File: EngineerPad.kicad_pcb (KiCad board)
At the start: 2 copper layers, 67 parts, among them J1 AVR ISP, SW1 SW_Push, SW10 SW_Push, SW11 SW_Push, SW12 SW_Push, SW13 SW_Push, SW14 SW_Push, SW15 SW_Push, SW16 SW_Push, SW17 SW_Push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

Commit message: layout change
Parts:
- moved F1 17.3 mm to (152.0, 51.8)
- moved C3 16.5 mm to (149.9, 45.0)
- moved D24 14.1 mm to (134.3, 51.2)
- moved D25 14.1 mm to (137.7, 51.2)
- moved USB1 4.48 mm to (138.0, 41.0)
- moved D26 2.93 mm to (149.5, 39.4)

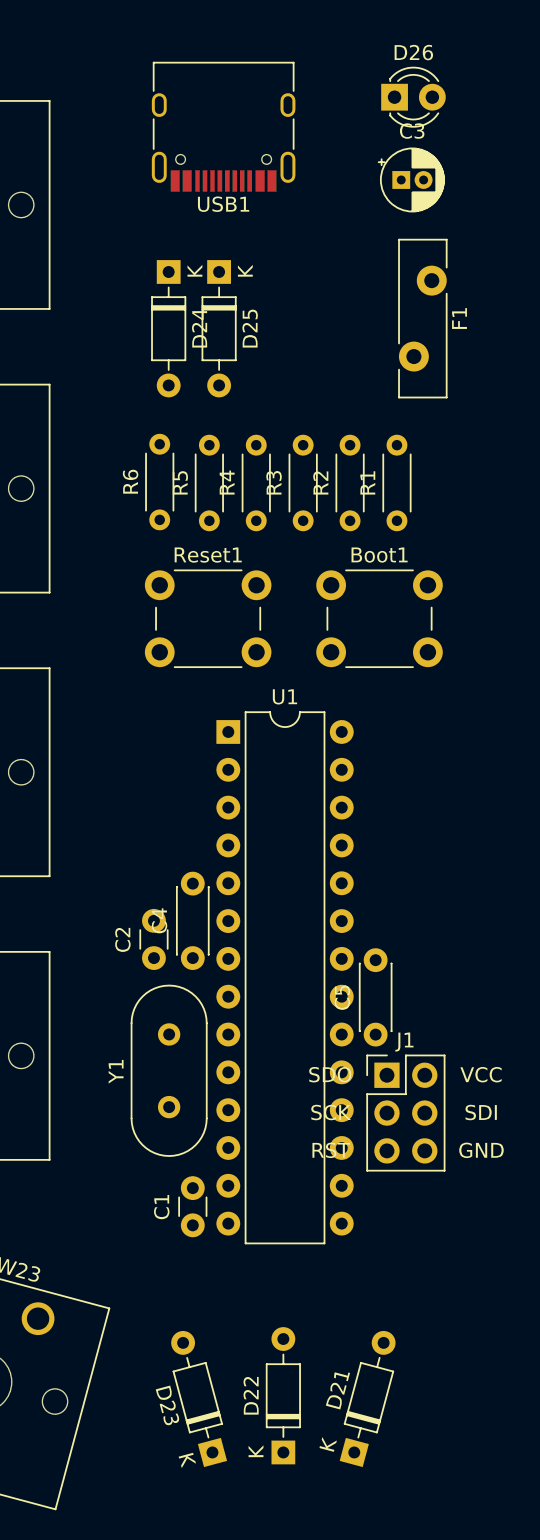
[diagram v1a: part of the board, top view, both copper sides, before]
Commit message: remove boot
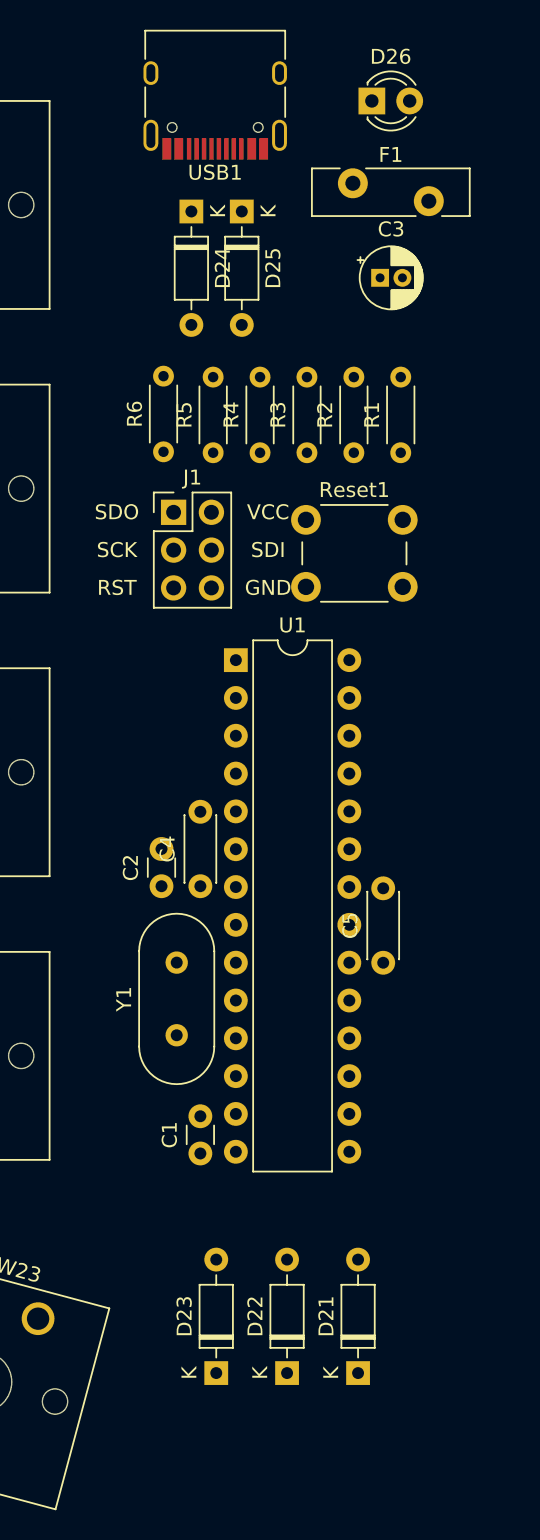
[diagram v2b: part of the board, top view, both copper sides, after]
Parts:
- removed Boot1: Boot, Button_Switch_THT:SW_PUSH_6mm
- moved J1 40.4 mm to (134.6, 67.3)
- moved Reset1 10.8 mm to (143.5, 67.8)
- moved F1 8.42 mm to (146.7, 45.2), turned to 0 degrees
- moved C3 6.72 mm to (148.5, 51.6)
- moved D23 5.34 mm to (137.5, 125.1), turned to 90 degrees
- moved D21 5.34 mm to (147.0, 125.1), turned to 90 degrees
- moved D22 5.34 mm to (142.2, 125.1)
- moved C1 4.85 mm to (136.4, 110.4)
- moved C5 4.85 mm to (148.7, 97.6)
- moved Y1 4.85 mm to (134.8, 102.4)
- moved C4 4.85 mm to (136.4, 92.4)
- moved C2 4.85 mm to (133.8, 92.4)
- moved U1 4.85 mm to (138.8, 77.2)
- moved R5 4.58 mm to (137.3, 63.3)
- moved R1 4.58 mm to (149.9, 63.3)
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
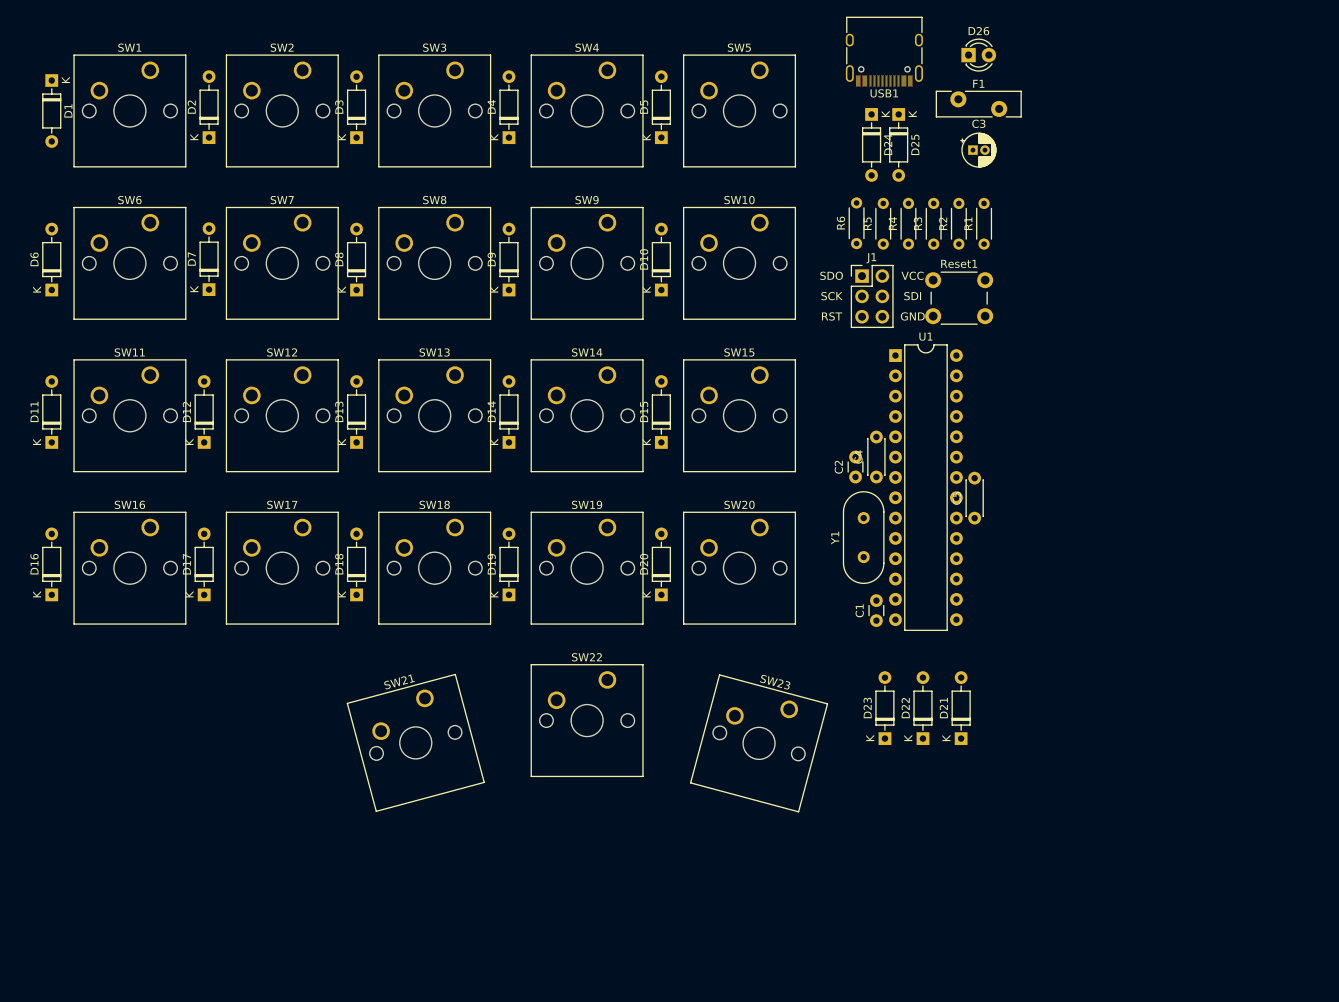
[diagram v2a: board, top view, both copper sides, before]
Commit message: switch to type a receptacle
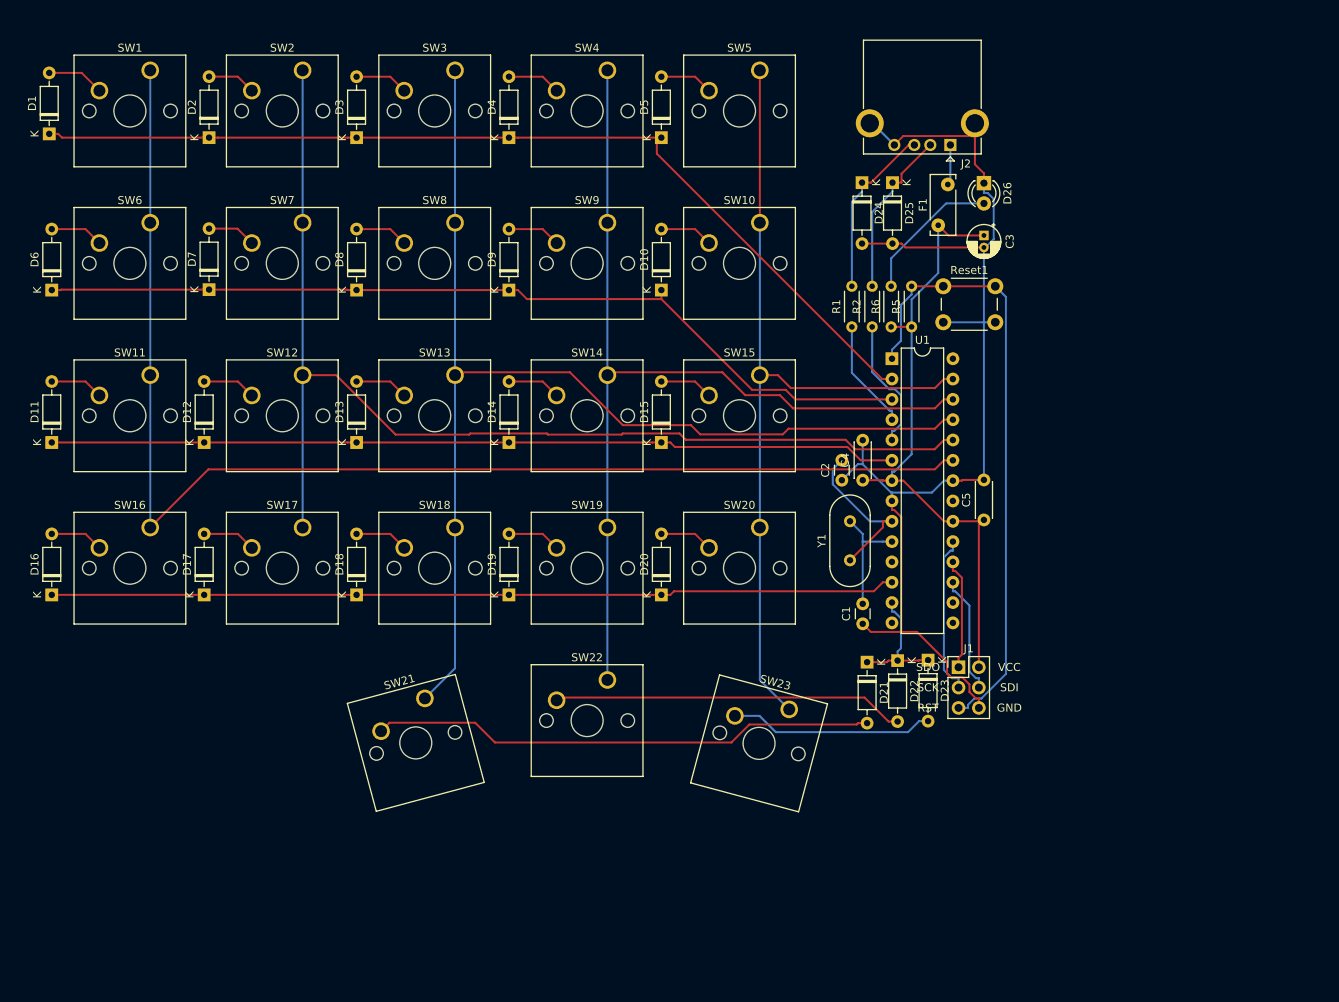
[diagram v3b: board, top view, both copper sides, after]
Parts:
- removed R3, R4: 5.1K, Resistor_THT:R_Axial_DIN0204_L3.6mm_D1.6mm_P5.08mm_Horizontal
- removed USB1: TYPE-C, JSA:USB_C_Receptacle_HRO_TYPE-C-31-M-12
- added J2: USB_A, Connector_USB:USB_A_CONNFLY_DS1095-WNR0, F.Cu at (145.7, 50.9)
- F1: footprint Fuse:Fuse_Bourns_MF-RG500 -> Fuse:Fuse_Bourns_MF-RHT050
- moved J1 50.4 mm to (146.7, 116.2)
- moved R1 19.5 mm to (133.3, 73.7)
- moved D26 16.1 mm to (149.9, 55.7), turned to 270 degrees
- moved F1 15.9 mm to (144.1, 61.0), turned to 90 degrees
- moved D21 15.1 mm to (135.3, 115.6), turned to 270 degrees
- moved R2 15.0 mm to (135.9, 73.7)
- moved R6 11.3 mm to (138.3, 73.7)
- moved D23 11.2 mm to (142.9, 115.3), turned to 270 degrees
- moved R5 10.9 mm to (140.8, 73.7)
- moved C3 10.8 mm to (149.9, 62.2), turned to 270 degrees
- moved D22 10.3 mm to (139.1, 115.4), turned to 270 degrees
- moved D24 8.60 mm to (134.6, 55.6)
- moved D25 8.55 mm to (138.4, 55.6)
- moved D1 6.68 mm to (33.0, 49.5), turned to 90 degrees
- moved C1 1.76 mm to (134.7, 110.8)
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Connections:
- net /DP renamed Net-(D24-Pad1)
- D25 pad 1: /DN -> Net-(D25-Pad1)
- F1 pad 2: /VSUB -> Net-(F1-Pad2)
- R2 pad 1: /DN -> D-
- R2 pad 2: D- -> Net-(D25-Pad1)
- U1 pad 11: Boot -> (no net)
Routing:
- net Col0: track 0.00 -> 161.0 mm
- net Col2: track 0.00 -> 146.4 mm
- net GND: track 0.00 -> 145.8 mm
- net Col1: track 0.00 -> 143.0 mm
- net Col3: track 0.00 -> 121.9 mm
- net Row0: track 0.00 -> 119.8 mm
- net Row1: track 0.00 -> 111.9 mm
- net Col4: track 0.00 -> 106.7 mm
- net Row2: track 0.00 -> 105.9 mm
- net Row3: track 0.00 -> 105.7 mm
- net +5V: track 0.00 -> 78.9 mm
- net Reset: track 0.00 -> 77.4 mm
- net Net-(D21-Pad2): track 0.00 -> 63.2 mm
- net Net-(D22-Pad2): track 0.00 -> 44.0 mm
- net Net-(D23-Pad2): track 0.00 -> 25.6 mm
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
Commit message: socket and low profile
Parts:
- SW21, SW22, SW23: footprint Button_Switch_Keyboard:SW_Cherry_MX_1.00u_PCB -> JSA:SW_PG1350
- U1: footprint Package_DIP:DIP-28_W7.62mm -> Package_DIP:DIP-28_W7.62mm_Socket
- moved SW23 8.26 mm to (119.4, 127.0)
- moved SW21 7.03 mm to (81.3, 127.0)
- moved SW22 5.73 mm to (100.1, 122.9)
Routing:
- net Col0: track 161.0 -> 0.00 mm
- net Col2: track 146.4 -> 0.00 mm
- net GND: track 145.8 -> 0.00 mm
- net Col1: track 143.0 -> 0.00 mm
- net Col3: track 121.9 -> 0.00 mm
- net Row0: track 119.8 -> 0.00 mm
- net Row1: track 111.9 -> 0.00 mm
- net Col4: track 106.7 -> 0.00 mm
- net Row2: track 105.9 -> 0.00 mm
- net Row3: track 105.7 -> 0.00 mm
- net +5V: track 78.9 -> 0.00 mm
- net Reset: track 77.4 -> 0.00 mm
- net Net-(D21-Pad2): track 63.2 -> 0.00 mm
- net Net-(D22-Pad2): track 44.0 -> 0.00 mm
- net Net-(D23-Pad2): track 25.6 -> 0.00 mm
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
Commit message: first layout
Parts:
- added R3: 1.5k, Resistor_THT:R_Axial_DIN0204_L3.6mm_D1.6mm_P5.08mm_Horizontal, F.Cu at (138.4, 72.4)
- moved D23 11.5 mm to (131.6, 117.3)
- moved D25 7.08 mm to (135.9, 62.2), turned to 90 degrees
- moved D24 6.73 mm to (133.3, 62.2), turned to 90 degrees
- moved Y1 5.05 mm to (133.3, 97.8), turned to 270 degrees
- moved D22 4.41 mm to (135.1, 117.3)
- moved D21 3.86 mm to (138.7, 117.3)
- moved R6 2.99 mm to (141.0, 72.4)
- moved R5 2.97 mm to (143.5, 72.4)
- moved Reset1 2.84 mm to (147.3, 67.3)
- moved C2 2.65 mm to (132.1, 90.2), turned to 270 degrees
- moved F1 1.91 mm to (142.2, 61.0)
- moved J1 1.88 mm to (145.8, 117.9)
- moved C3 1.80 mm to (148.6, 61.0)
- moved D26 1.67 mm to (148.6, 54.6)
- moved R1 1.27 mm to (133.3, 72.4)
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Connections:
- net Net-(D24-Pad1) renamed /DP
- net Net-(D25-Pad1) renamed /DN
- J1 pad 1: SDO -> Row1
- J1 pad 3: SCK -> Row0
- J1 pad 4: SDI -> Row2
- U1 pad 12: Row3 -> (no net)
- U1 pad 13: Row4 -> (no net)
- U1 pad 15: (no net) -> Row4
- U1 pad 16: (no net) -> Row3
- U1 pad 17: SDI -> Row2
- U1 pad 18: SDO -> Row1
- U1 pad 19: SCK -> Row0
- U1 pad 2: Row0 -> (no net)
- U1 pad 23: Col0 -> Col4
- U1 pad 24: Col1 -> Col3
- U1 pad 26: Col3 -> Col1
- U1 pad 27: Col4 -> Col0
- U1 pad 3: Row1 -> (no net)
- U1 pad 4: D+ -> D-
- U1 pad 5: D- -> D+
- U1 pad 6: Row2 -> (no net)
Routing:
- net Col0: track 0.00 -> 239.0 mm
- net Col1: track 0.00 -> 227.1 mm
- net Row0: track 0.00 -> 213.0 mm
- net Col2: track 0.00 -> 210.4 mm
- net Col3: track 0.00 -> 188.7 mm
- net Row1: track 0.00 -> 186.4 mm
- net Col4: track 0.00 -> 180.9 mm
- net Reset: track 0.00 -> 156.5 mm
- net Row2: track 0.00 -> 155.7 mm
- net Row3: track 0.00 -> 119.8 mm
- net +5V: track 0.00 -> 90.3 mm
- net Net-(D21-Pad2): track 0.00 -> 64.8 mm
- net Net-(D22-Pad2): track 0.00 -> 45.0 mm
- net /DN: track 0.00 -> 23.3 mm
- net Net-(D23-Pad2): track 0.00 -> 20.7 mm
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- added copper zone on B.Cu, net GND
- added copper zone on F.Cu, net GND
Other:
- net class Power added: clearance 0.2, trace_width 0.5, via_dia 0.8, via_drill 0.4

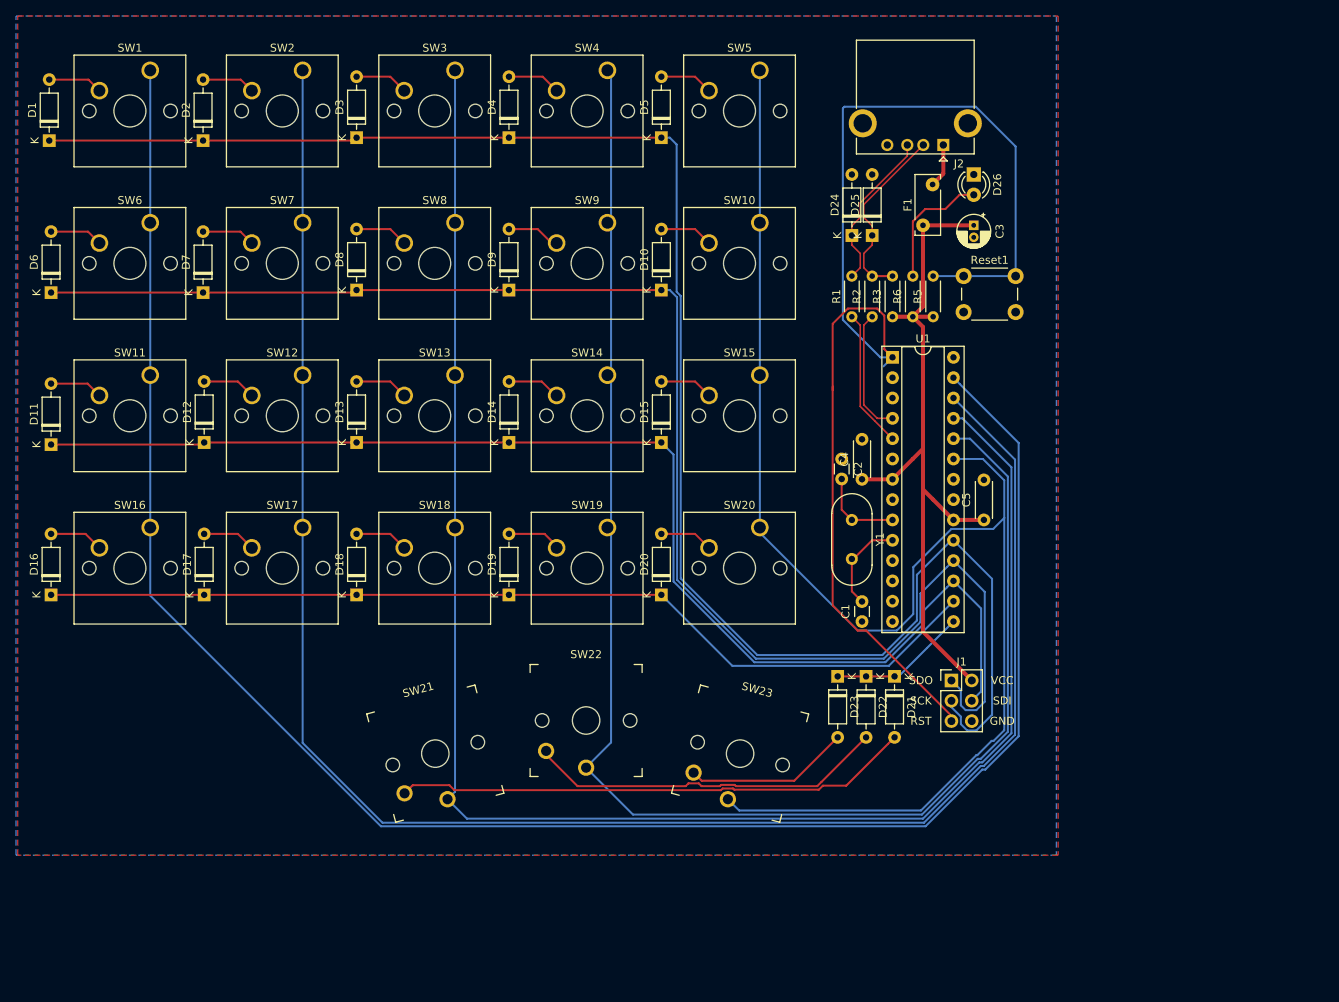
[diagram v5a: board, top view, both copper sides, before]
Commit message: Form factor 因為要做成5mm邊框切齊鍵帽，因此PCB從鍵帽處內縮1mm，外殼預計是5mm。
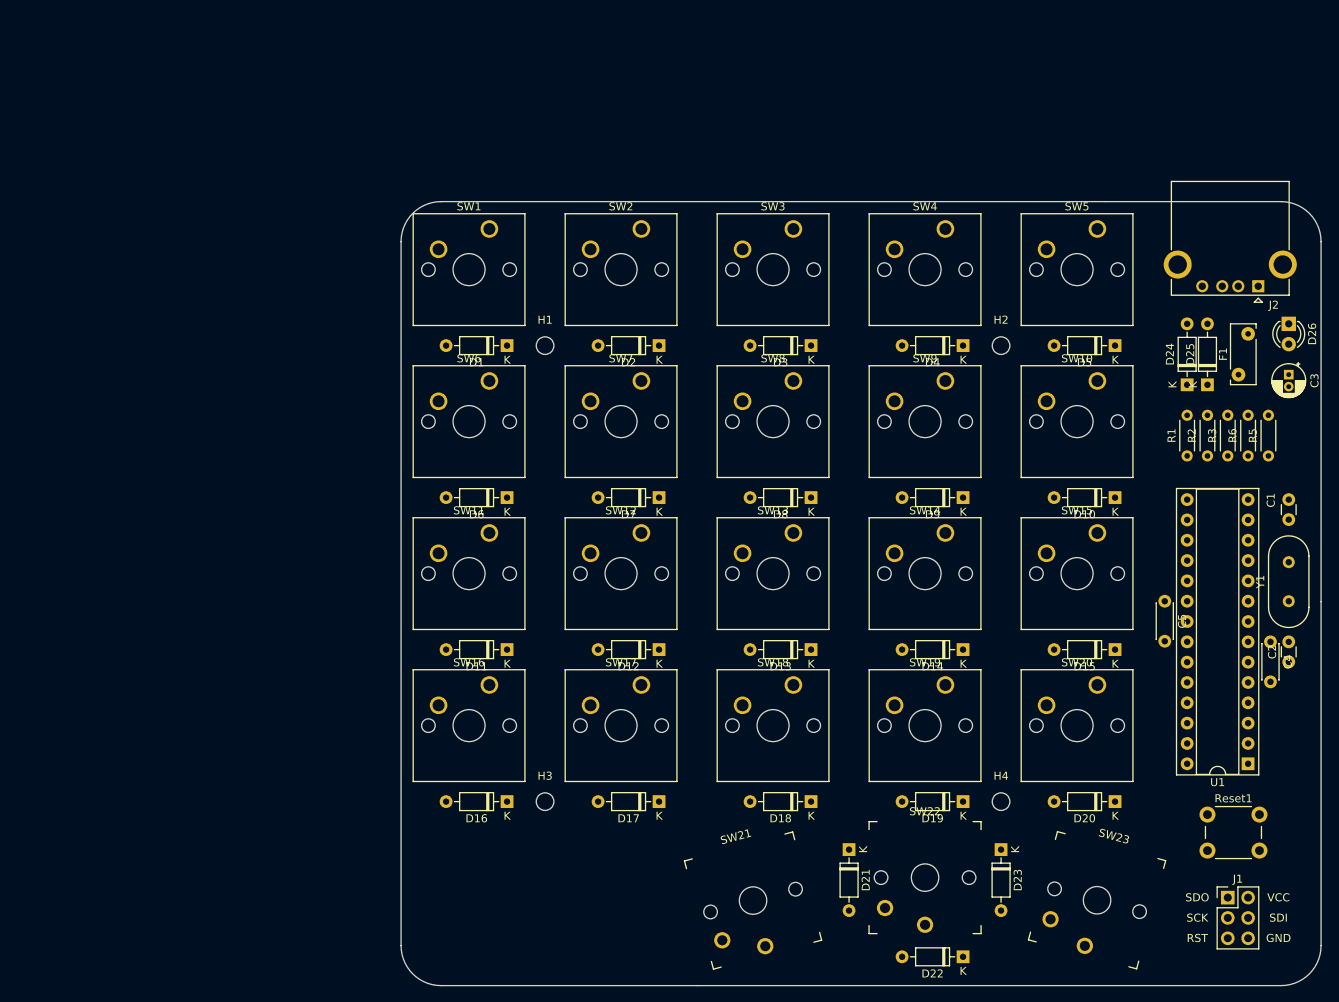
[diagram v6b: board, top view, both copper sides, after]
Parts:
- added H1: MountingHole, MountingHole:MountingHole_2.2mm_M2, F.Cu at (95.0, 76.0)
- added H2: MountingHole, MountingHole:MountingHole_2.2mm_M2, F.Cu at (152.0, 76.0)
- added H3: MountingHole, MountingHole:MountingHole_2.2mm_M2, F.Cu at (95.0, 133.0)
- added H4: MountingHole, MountingHole:MountingHole_2.2mm_M2, F.Cu at (152.0, 133.0)
- moved Reset1 73.9 mm to (177.8, 134.6)
- moved U1 67.5 mm to (182.9, 128.3), turned to 180 degrees
- moved D1 62.7 mm to (90.2, 76.0), turned to 180 degrees
- moved D16 62.6 mm to (90.2, 133.0), turned to 180 degrees
- moved D11 62.5 mm to (90.2, 114.0), turned to 180 degrees
- moved D2 62.5 mm to (109.2, 76.0), turned to 180 degrees
- moved D6 62.5 mm to (90.2, 95.0), turned to 180 degrees
- moved D7 62.5 mm to (109.2, 95.0), turned to 180 degrees
- moved D12 62.5 mm to (109.2, 114.0), turned to 180 degrees
- moved D3 62.5 mm to (128.2, 76.0), turned to 180 degrees
- moved D17 62.5 mm to (109.2, 133.0), turned to 180 degrees
- moved D8 62.5 mm to (128.2, 95.0), turned to 180 degrees
- moved D13 62.4 mm to (128.2, 114.0), turned to 180 degrees
- moved D4 62.4 mm to (147.2, 76.0), turned to 180 degrees
- moved D18 62.4 mm to (128.2, 133.0), turned to 180 degrees
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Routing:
- net Col0: track 239.0 -> 0.00 mm
- net Col1: track 227.1 -> 0.00 mm
- net Row0: track 213.0 -> 0.00 mm
- net Col2: track 210.4 -> 0.00 mm
- net Col3: track 188.7 -> 0.00 mm
- net Row1: track 186.4 -> 0.00 mm
- net Col4: track 180.9 -> 0.00 mm
- net Reset: track 156.5 -> 0.00 mm
- net Row2: track 155.7 -> 0.00 mm
- net Row3: track 119.8 -> 0.00 mm
- net +5V: track 90.3 -> 0.00 mm
- net Net-(D21-Pad2): track 64.8 -> 0.00 mm
- net Net-(D22-Pad2): track 45.0 -> 0.00 mm
- net /DN: track 23.3 -> 0.00 mm
- net Net-(D23-Pad2): track 20.7 -> 0.00 mm
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- removed copper zone on B.Cu, net GND
- removed copper zone on F.Cu, net GND
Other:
- board outline added: 115 x 98 mm
- board text added: "Keyswitch: 19mm Electronic Component: 100mil(0.254mm)"
